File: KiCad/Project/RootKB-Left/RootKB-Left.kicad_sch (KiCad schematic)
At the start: 70 parts, among them J1 OLED-128x32, SW1 Switch, U1 Arduino_Pro_Micro, U2 TRRS

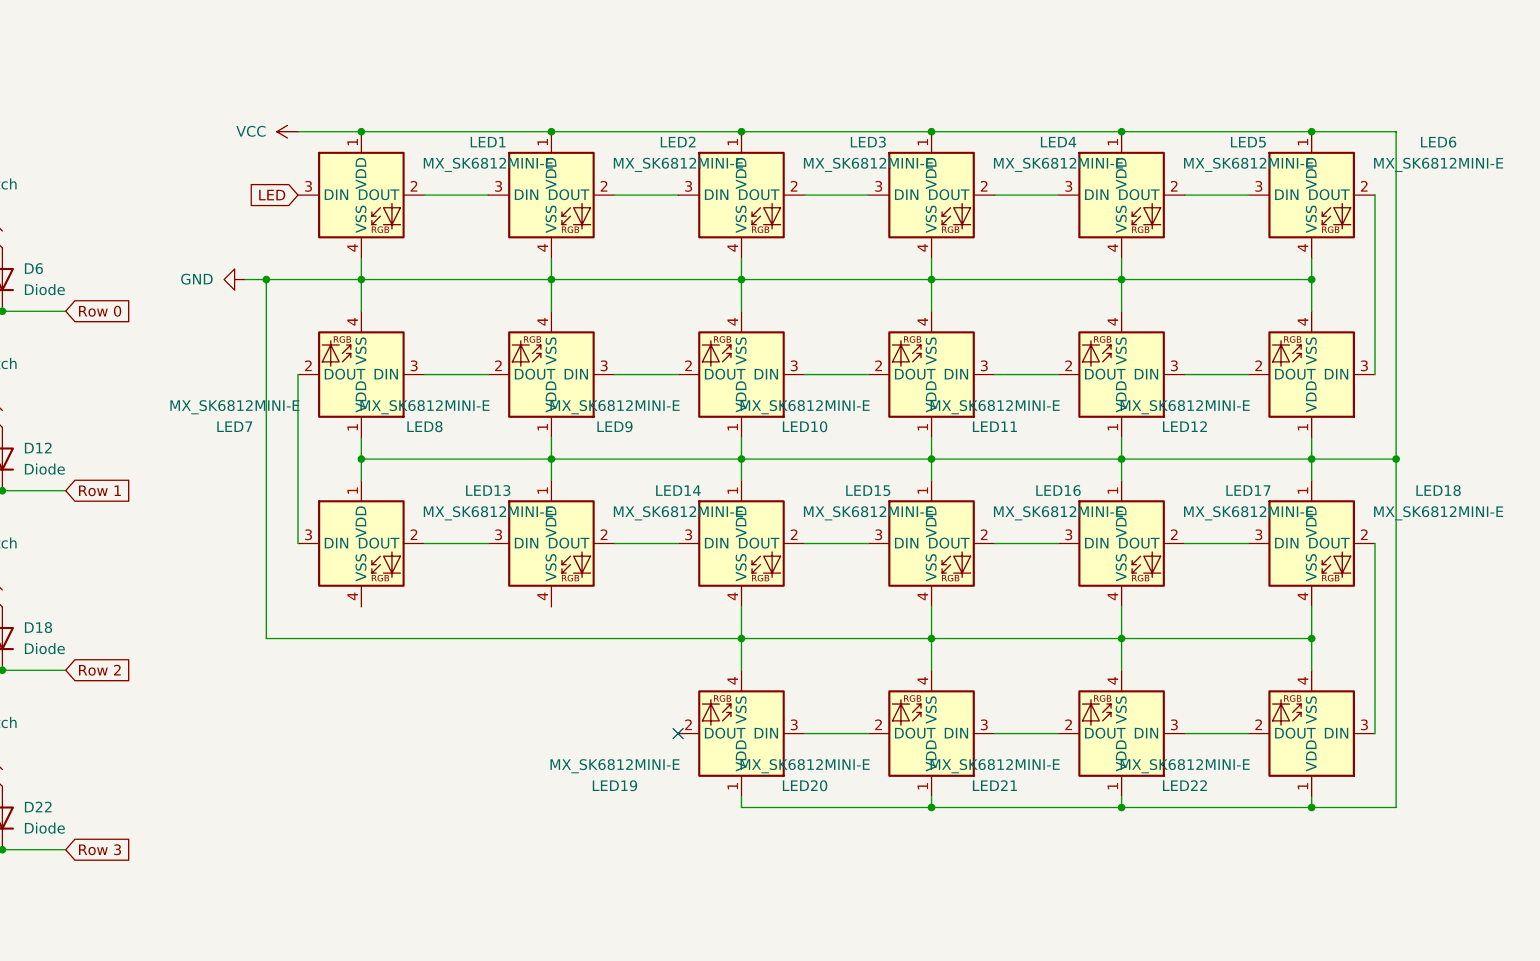
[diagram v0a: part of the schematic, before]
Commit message: route left
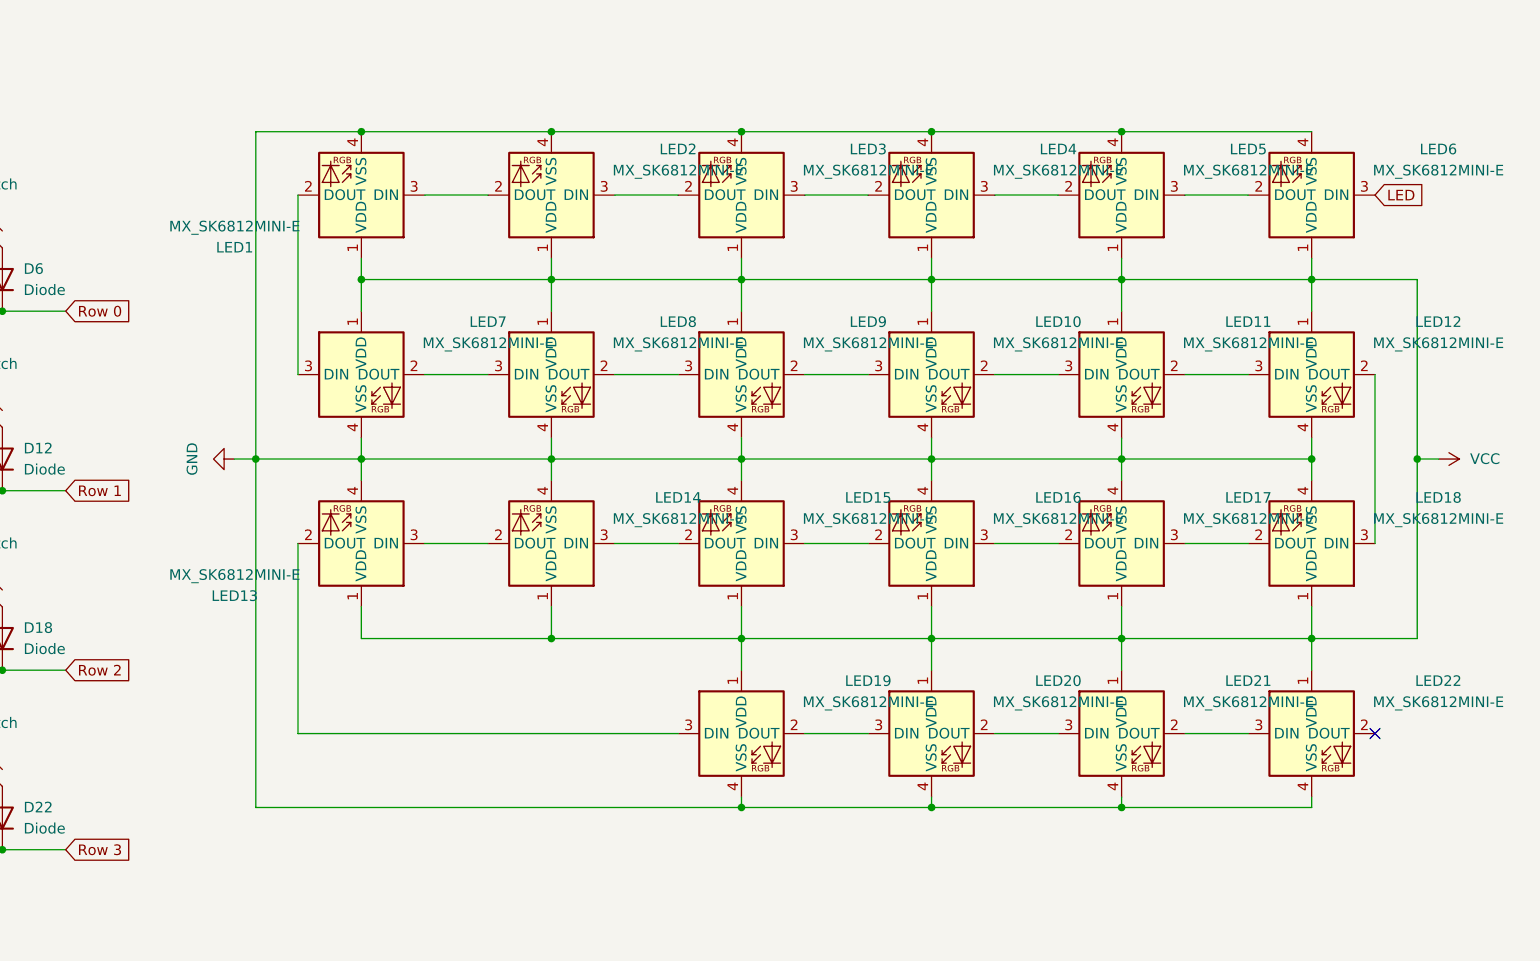
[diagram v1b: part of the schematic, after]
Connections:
- net GND: now also LED13.4 (VSS), LED14.4 (VSS)
- net LED: now also LED6.3 (DIN); no longer LED1.3 (DIN)
- net at LED2.2 (DOUT): now also LED1.3 (DIN); no longer LED3.3 (DIN)
- net at LED2.3 (DIN): now also LED3.2 (DOUT); no longer LED1.2 (DOUT)
- net at LED21.2 (DOUT): now also LED22.3 (DIN); no longer LED20.3 (DIN)
- net at LED21.3 (DIN): now also LED20.2 (DOUT); no longer LED22.2 (DOUT)
- net at LED9.2 (DOUT): now also LED10.3 (DIN); no longer LED8.3 (DIN)
- net at LED9.3 (DIN): now also LED8.2 (DOUT); no longer LED10.2 (DOUT)
- net at LED7.3 (DIN): now also LED1.2 (DOUT); no longer LED8.2 (DOUT)
- net at LED7.2 (DOUT): now also LED8.3 (DIN); no longer LED13.3 (DIN)
- net at LED5.2 (DOUT): now also LED4.3 (DIN); no longer LED6.3 (DIN)
- net at LED5.3 (DIN): now also LED6.2 (DOUT); no longer LED4.2 (DOUT)
- net at LED11.2 (DOUT): now also LED12.3 (DIN); no longer LED10.3 (DIN)
- net at LED11.3 (DIN): now also LED10.2 (DOUT); no longer LED12.2 (DOUT)
- net at LED17.2 (DOUT): now also LED16.3 (DIN); no longer LED18.3 (DIN)
- net at LED17.3 (DIN): now also LED18.2 (DOUT); no longer LED16.2 (DOUT)
- net at LED15.2 (DOUT): now also LED14.3 (DIN); no longer LED16.3 (DIN)
- net at LED13.2 (DOUT): now also LED19.3 (DIN); no longer LED14.3 (DIN)
- net at LED19.2 (DOUT): now also LED20.3 (DIN)
- net at LED15.3 (DIN): now also LED16.2 (DOUT); no longer LED14.2 (DOUT)
- new net: LED13.3 (DIN), LED14.2 (DOUT)
- new net: LED12.2 (DOUT), LED18.3 (DIN)
- new net: LED3.3 (DIN), LED4.2 (DOUT)
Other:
- moved on the sheet: LED1, LED10, LED11, LED12, LED13, LED14, LED15, LED16, LED17, LED18, LED19, LED2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

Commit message: routing left
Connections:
- net Column 1: now also U1.13 (10/PB6); no longer U1.16 (15/PB1)
- net Column 2: now also U1.14 (16/PB2); no longer U1.15 (14/PB3)
- net Column 3: now also U1.15 (14/PB3); no longer U1.14 (16/PB2)
- net Column 4: now also U1.16 (15/PB1); no longer U1.13 (10/PB6)

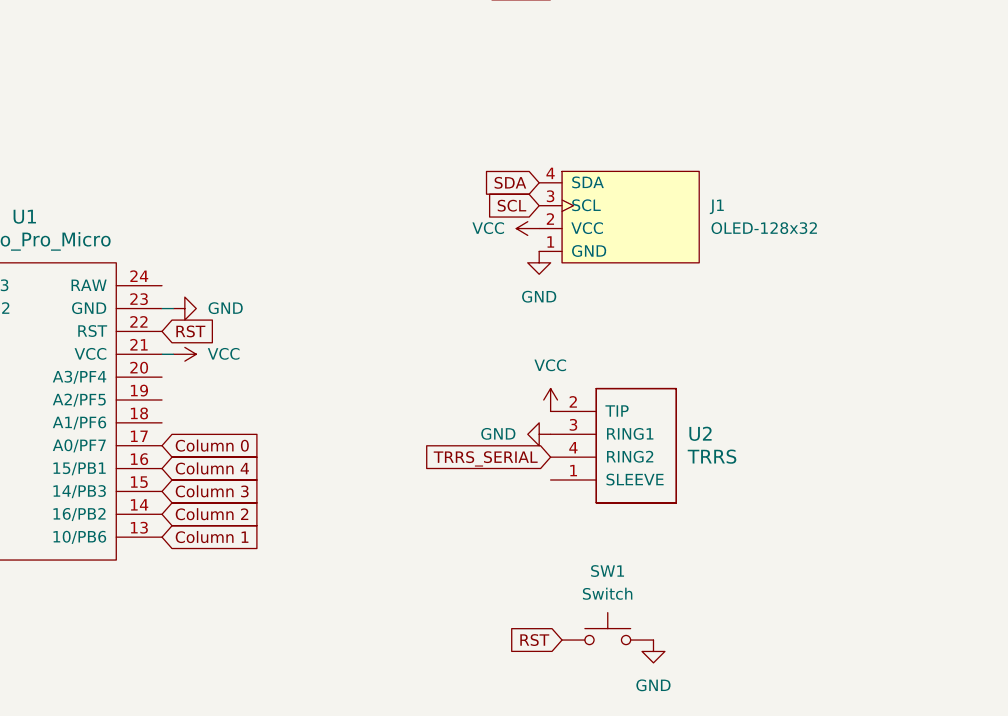
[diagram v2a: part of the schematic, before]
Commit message: remove reset button
also use real Arduino ProMicro dimensions
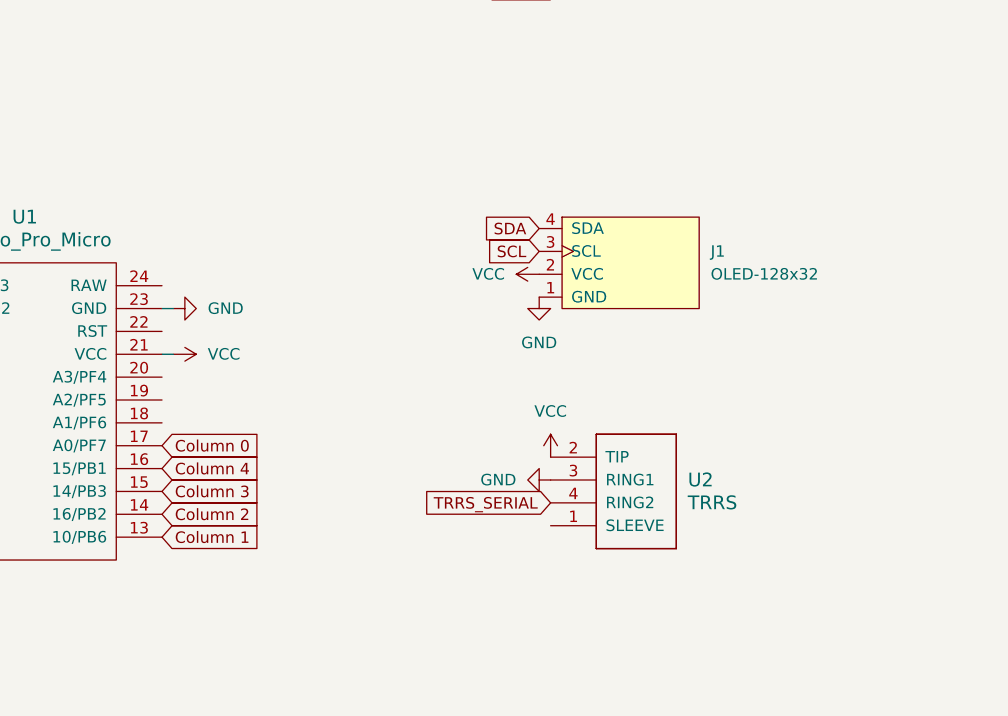
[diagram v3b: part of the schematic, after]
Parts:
- removed SW1: Switch, ScottoKeebs_Components:Button_MJTP1250, symbol ScottoKeebs:Placeholder_Switch
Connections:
- net RST: no longer names the net of U1.22 (RST)
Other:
- moved on the sheet: J1, U2

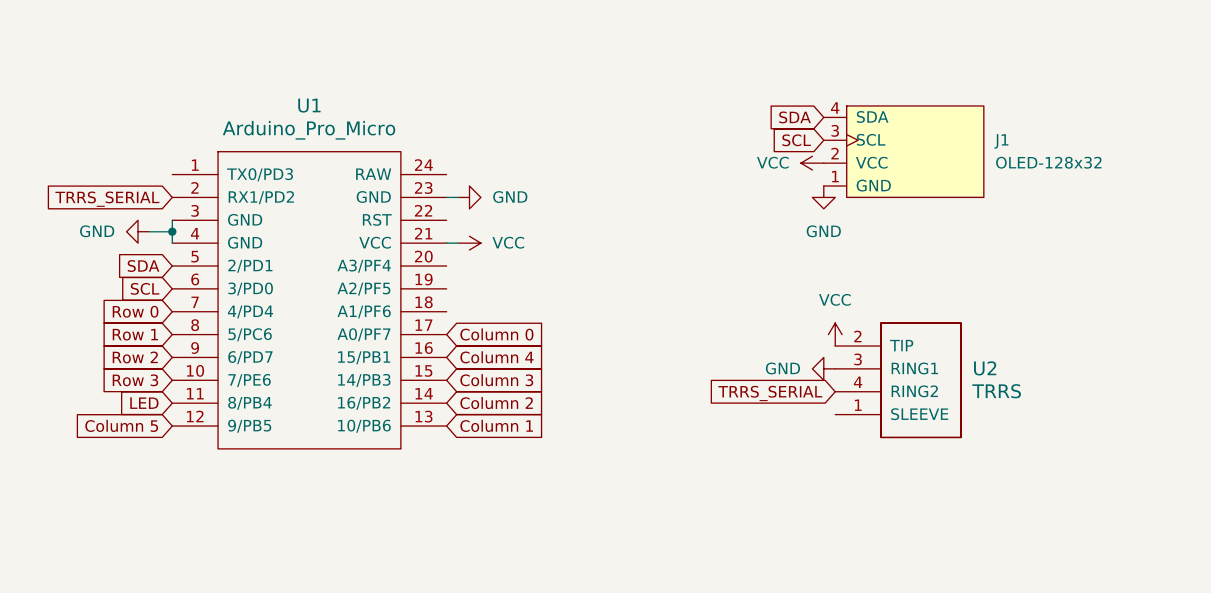
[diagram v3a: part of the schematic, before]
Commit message: use UART
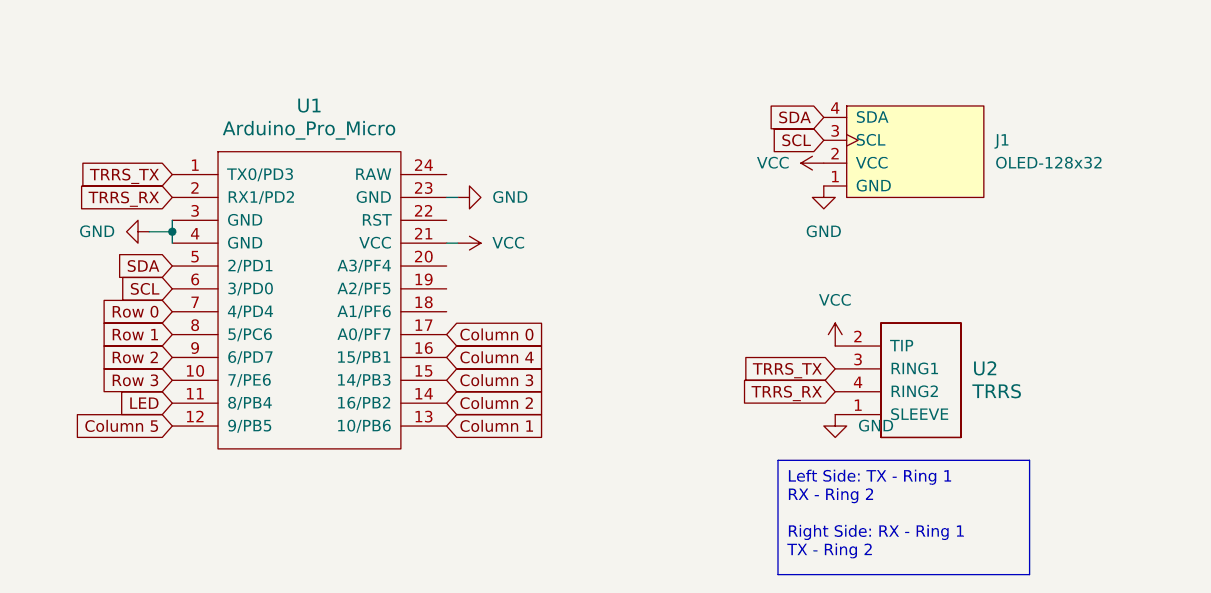
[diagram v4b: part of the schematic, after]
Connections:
- net GND: now also U2.1 (SLEEVE); no longer U2.3 (RING1)
- net TRRS_TX: now reaches U1.1 (TX0/PD3)
- net TRRS_TX: now also U2.3 (RING1)
- net TRRS_SERIAL renamed TRRS_RX
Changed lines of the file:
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@@
 		)
 	)
+	(text_box "Left Side: TX - Ring 1\n           RX - Ring 2\n\nRight Side: RX - Ring 1\n            TX - Ring 2"
+		(exclude_from_sim no)
+		(at 101.6 180.34 0)
+		(size 27.94 12.7)
+		(stroke
+			(width 0)
+			(type default)
+		)
+		(fill
+			(type none)
+		)
+		(effects
+			(font
+				(size 1.27 1.27)
+			)
+			(justify left top)
+		)
+	)
 	(global_label "Column 5"
 		(shape input)
@@
 		)
 	)
+	(global_label "TRRS_RX"
+		(shape input)
+		(at 34.29 151.13 180)
+		(fields_autoplaced yes)
+		(effects
+			(font
+				(size 1.27 1.27)
+			)
+			(justify right)
+		)
+		(property "Intersheetrefs" "${INTERSHEET_REFS}"
+			(at 23.1406 151.13 0)
+			(effects
+				(font
+					(size 1.27 1.27)
+				)
+				(justify right)
+				(hide yes)
+			)
+		)
+	)
 	(global_label "Column 5"
 		(shape input)
@@
 		)
 	)
-	(global_label "TRRS_SERIAL"
+	(global_label "TRRS_RX"
 		(shape input)
 		(at 107.95 172.72 180)
@@
 		)
 	)
+	(global_label "TRRS_TX"
+		(shape input)
+		(at 107.95 170.18 180)
+		(fields_autoplaced yes)
+		(effects
+			(font
+				(size 1.27 1.27)
+			)
+			(justify right)
+		)
+		(property "Intersheetrefs" "${INTERSHEET_REFS}"
+			(at 97.103 170.18 0)
+			(effects
+				(font
+					(size 1.27 1.27)
+				)
+				(justify right)
+				(hide yes)
+			)
+		)
+	)
 	(global_label "Column 1"
 		(shape input)
@@
 		)
 	)
+	(global_label "TRRS_TX"
+		(shape input)
+		(at 34.29 148.59 180)
+		(fields_autoplaced yes)
+		(effects
+			(font
+				(size 1.27 1.27)
+			)
+			(justify right)
+		)
+		(property "Intersheetrefs" "${INTERSHEET_REFS}"
+			(at 23.443 148.59 0)
+			(effects
+				(font
+					(size 1.27 1.27)
+				)
+				(justify right)
+				(hide yes)
+			)
+		)
+	)
 	(global_label "Column 4"
 		(shape input)
@@
 		)
 	)
-	(global_label "TRRS_SERIAL"
-		(shape input)
-		(at 34.29 151.13 180)
-		(fields_autoplaced yes)
-		(effects
-			(font
-				(size 1.27 1.27)
-			)
-			(justify right)
-		)
-		(property "Intersheetrefs" "${INTERSHEET_REFS}"
-			(at 23.1406 151.13 0)
-			(effects
-				(font
-					(size 1.27 1.27)
-				)
-				(justify right)
-				(hide yes)
-			)
-		)
-	)
 	(global_label "Row 1"
 		(shape input)
@@
 	(symbol
 		(lib_id "power:GND")
-		(at 107.95 170.18 270)
+		(at 107.95 175.26 0)
 		(unit 1)
 		(exclude_from_sim no)
@@
 		(fields_autoplaced yes)
 		(property "Reference" "#PWR02"
-			(at 101.6 170.18 0)
+			(at 107.95 181.61 0)
 			(effects
 				(font
@@
 		)
 		(property "Value" "GND"
-			(at 104.14 170.1799 90)
+			(at 110.49 176.5299 0)
 			(effects
 				(font
 					(size 1.27 1.27)
 				)
-				(justify right)
+				(justify left)
 			)
 		)
 		(property "Footprint" ""
-			(at 107.95 170.18 0)
+			(at 107.95 175.26 0)
 			(effects
 				(font
@@
 		)
 		(property "Datasheet" ""
-			(at 107.95 170.18 0)
+			(at 107.95 175.26 0)
 			(effects
 				(font
@@
 		)
 		(property "Description" "Power symbol creates a global label with name \"GND\" , ground"
-			(at 107.95 170.18 0)
+			(at 107.95 175.26 0)
 			(effects
 				(font
